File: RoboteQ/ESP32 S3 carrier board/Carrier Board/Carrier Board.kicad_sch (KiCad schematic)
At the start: 2 parts, among them J1 Conn_01x22_Pin, J2 Conn_01x22_Pin

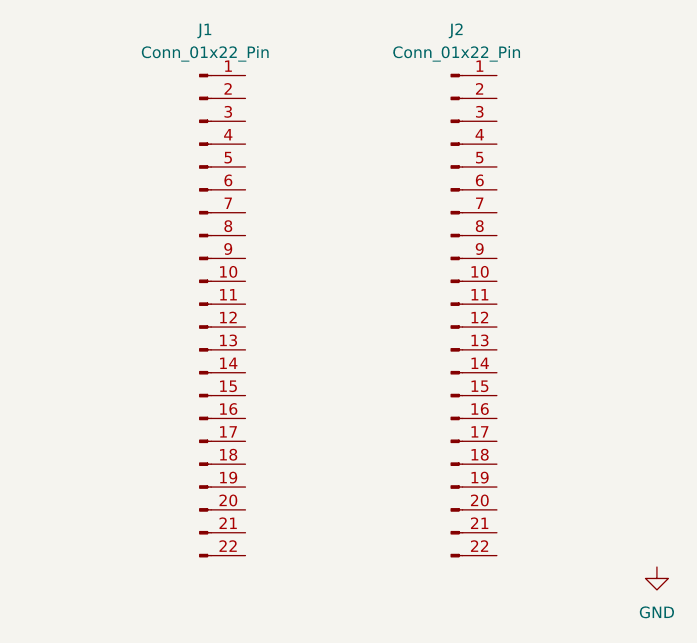
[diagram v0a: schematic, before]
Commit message: Added firmware chapter in technical review.
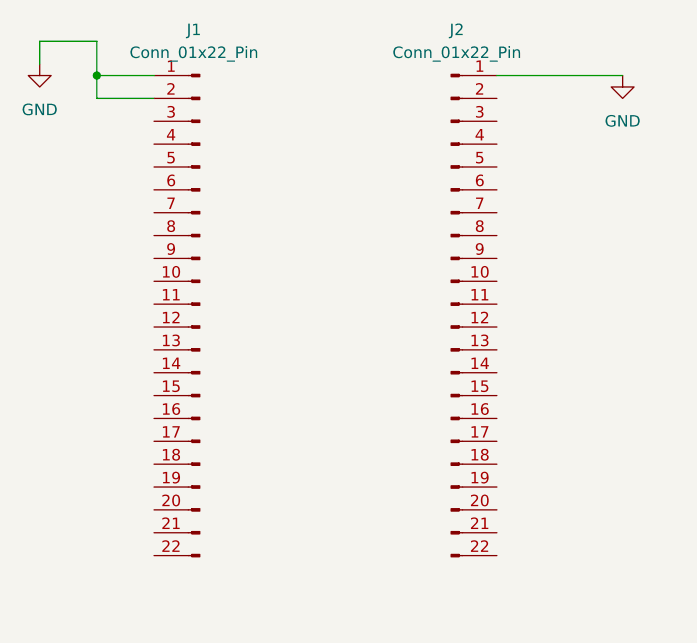
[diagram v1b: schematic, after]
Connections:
- net GND: now also J1.1 (Pin_1), J1.2 (Pin_2), J2.1 (Pin_1)
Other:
- moved on the sheet: J1
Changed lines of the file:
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@@
 	(generator_version "10.0")
 	(paper "A4")
+	(junction
+		(at 115.57 31.75)
+		(diameter 0)
+		(color 0 0 0 0)
+	)
+	(wire
+		(pts
+			(xy 121.92 34.29) (xy 115.57 34.29)
+		)
+		(stroke
+			(width 0)
+			(type default)
+		)
+	)
+	(wire
+		(pts
+			(xy 115.57 34.29) (xy 115.57 31.75)
+		)
+		(stroke
+			(width 0)
+			(type default)
+		)
+	)
+	(wire
+		(pts
+			(xy 121.92 31.75) (xy 115.57 31.75)
+		)
+		(stroke
+			(width 0)
+			(type default)
+		)
+	)
+	(wire
+		(pts
+			(xy 115.57 27.94) (xy 109.22 27.94)
+		)
+		(stroke
+			(width 0)
+			(type default)
+		)
+	)
+	(wire
+		(pts
+			(xy 160.02 31.75) (xy 173.99 31.75)
+		)
+		(stroke
+			(width 0)
+			(type default)
+		)
+	)
+	(wire
+		(pts
+			(xy 115.57 31.75) (xy 115.57 27.94)
+		)
+		(stroke
+			(width 0)
+			(type default)
+		)
+	)
+	(wire
+		(pts
+			(xy 109.22 27.94) (xy 109.22 30.48)
+		)
+		(stroke
+			(width 0)
+			(type default)
+		)
+	)
 	(symbol
 		(lib_id "Connector:Conn_01x22_Pin")
 		(at 127 57.15 0)
+		(mirror y)
 		(unit 1)
 		(body_style 1)
@@
 		(in_pos_files yes)
 		(dnp no)
-		(fields_autoplaced yes)
 		(property "Reference" "J1"
-			(at 127.635 26.67 0)
+			(at 126.365 26.67 0)
 			(show_name no)
 			(do_not_autoplace no)
@@
 		)
 		(property "Value" "Conn_01x22_Pin"
-			(at 127.635 29.21 0)
+			(at 126.365 29.21 0)
 			(show_name no)
 			(do_not_autoplace no)
@@
 	(symbol
 		(lib_id "power:GND")
-		(at 177.8 86.36 0)
+		(at 109.22 30.48 0)
 		(unit 1)
 		(body_style 1)
@@
 		(fields_autoplaced yes)
 		(property "Reference" "#PWR01"
-			(at 177.8 92.71 0)
+			(at 109.22 36.83 0)
 			(hide yes)
 			(show_name no)
@@
 		)
 		(property "Value" "GND"
-			(at 177.8 91.44 0)
+			(at 109.22 35.56 0)
 			(show_name no)
 			(do_not_autoplace no)
@@
 		)
 		(property "Footprint" ""
-			(at 177.8 86.36 0)
+			(at 109.22 30.48 0)
 			(hide yes)
 			(show_name no)
@@
 		)
 		(property "Datasheet" ""
-			(at 177.8 86.36 0)
+			(at 109.22 30.48 0)
 			(hide yes)
 			(show_name no)
@@
 		)
 		(property "Description" "Power symbol creates a global label with name \"GND\" , ground"
-			(at 177.8 86.36 0)
+			(at 109.22 30.48 0)
 			(hide yes)
 			(show_name no)
@@
 					(unit 1)
 				)
+			)
+		)
+	)
+	(symbol
+		(lib_id "power:GND")
+		(at 173.99 31.75 0)
+		(unit 1)
+		(body_style 1)
+		(exclude_from_sim no)
+		(in_bom yes)
+		(on_board yes)
+		(in_pos_files yes)
+		(dnp no)
+		(fields_autoplaced yes)
+		(property "Reference" "#PWR02"
+			(at 173.99 38.1 0)
+			(hide yes)
+			(show_name no)
+			(do_not_autoplace no)
+			(effects
+				(font
+					(size 1.27 1.27)
+				)
+			)
+		)
+		(property "Value" "GND"
+			(at 173.99 36.83 0)
+			(show_name no)
+			(do_not_autoplace no)
+			(effects
+				(font
+					(size 1.27 1.27)
+				)
+			)
+		)
+		(property "Footprint" ""
+			(at 173.99 31.75 0)
+			(hide yes)
+			(show_name no)
+			(do_not_autoplace no)
+			(effects
+				(font
+					(size 1.27 1.27)
+				)
+			)
+		)
+		(property "Datasheet" ""
+			(at 173.99 31.75 0)
+			(hide yes)
+			(show_name no)
+			(do_not_autoplace no)
+			(effects
+				(font
+					(size 1.27 1.27)
+				)
+			)
+		)
+		(property "Description" "Power symbol creates a global label with name \"GND\" , ground"
+			(at 173.99 31.75 0)
+			(hide yes)
+			(show_name no)
+			(do_not_autoplace no)
+			(effects
+				(font
+					(size 1.27 1.27)
+				)
+			)
+		)
+		(pin "1"
+		)
+		(instances
+			(project "Carrier Board"
+				(path "/79d6ac5f-a939-4d7b-bf01-1a47a4c6b5a0"
+					(reference "#PWR02")
+					(unit 1)
+				)
